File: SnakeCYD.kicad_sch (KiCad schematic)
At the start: 1 part, among them U2 TFT_320x240

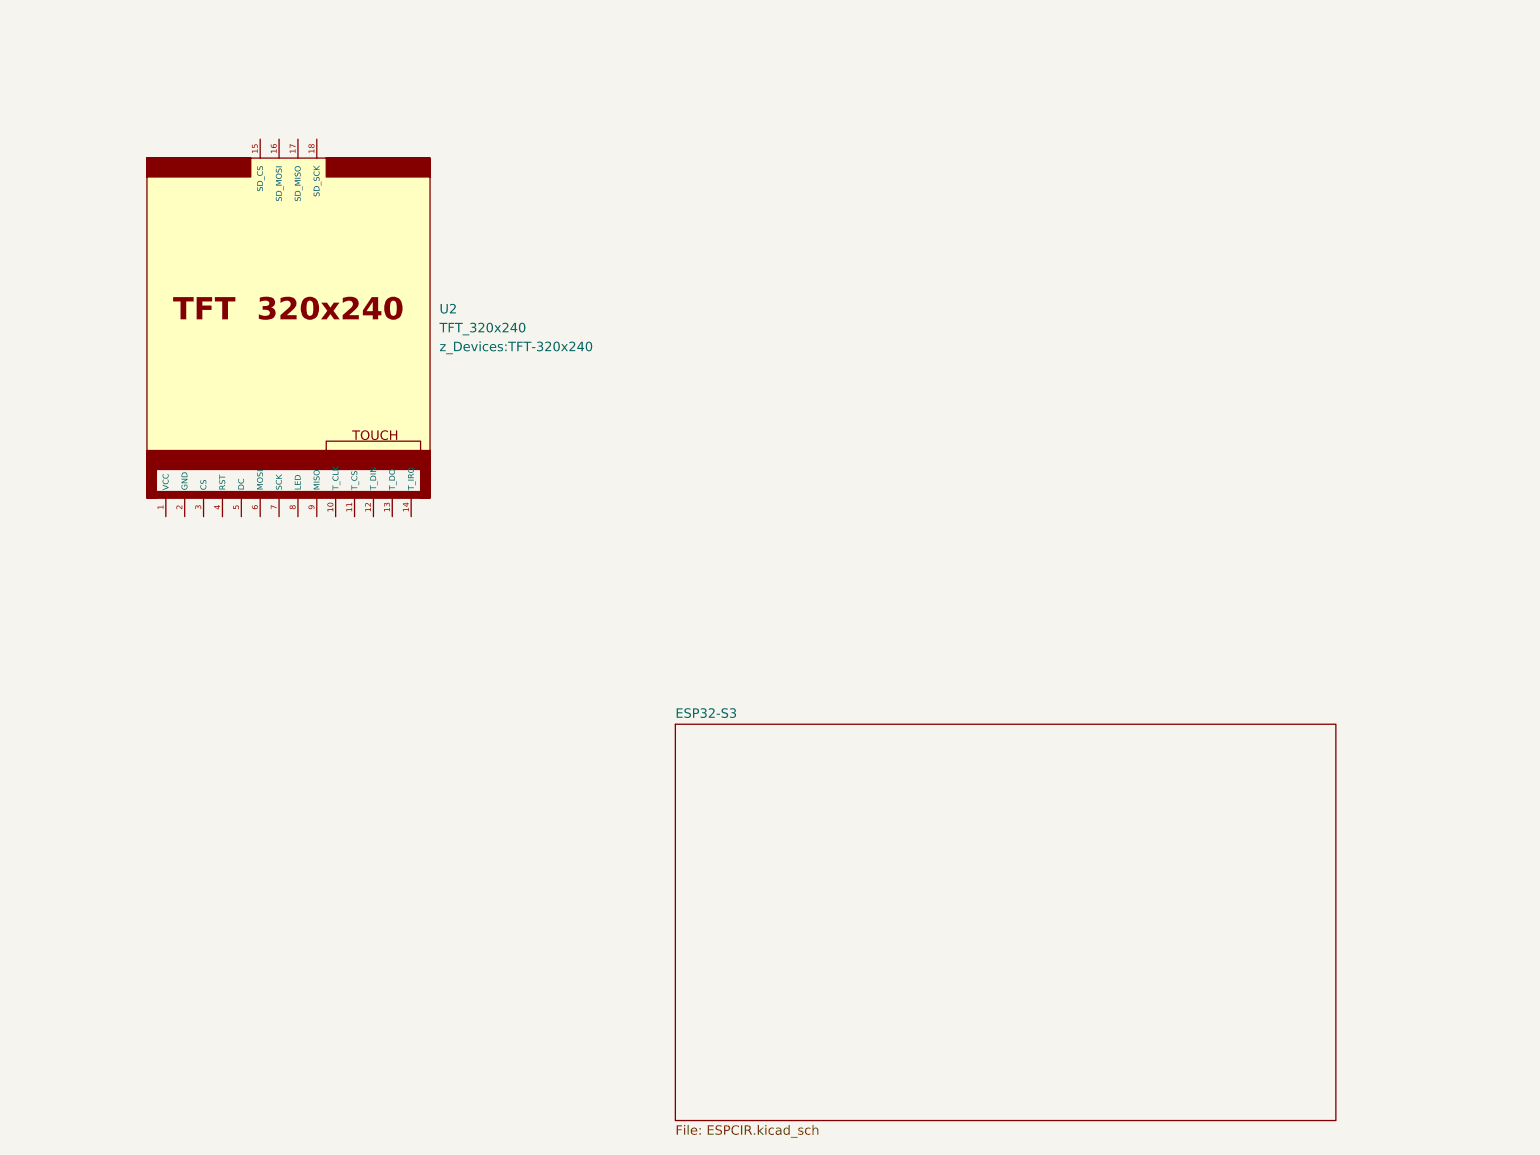
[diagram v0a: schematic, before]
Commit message: Wired the tft screen (Schem)
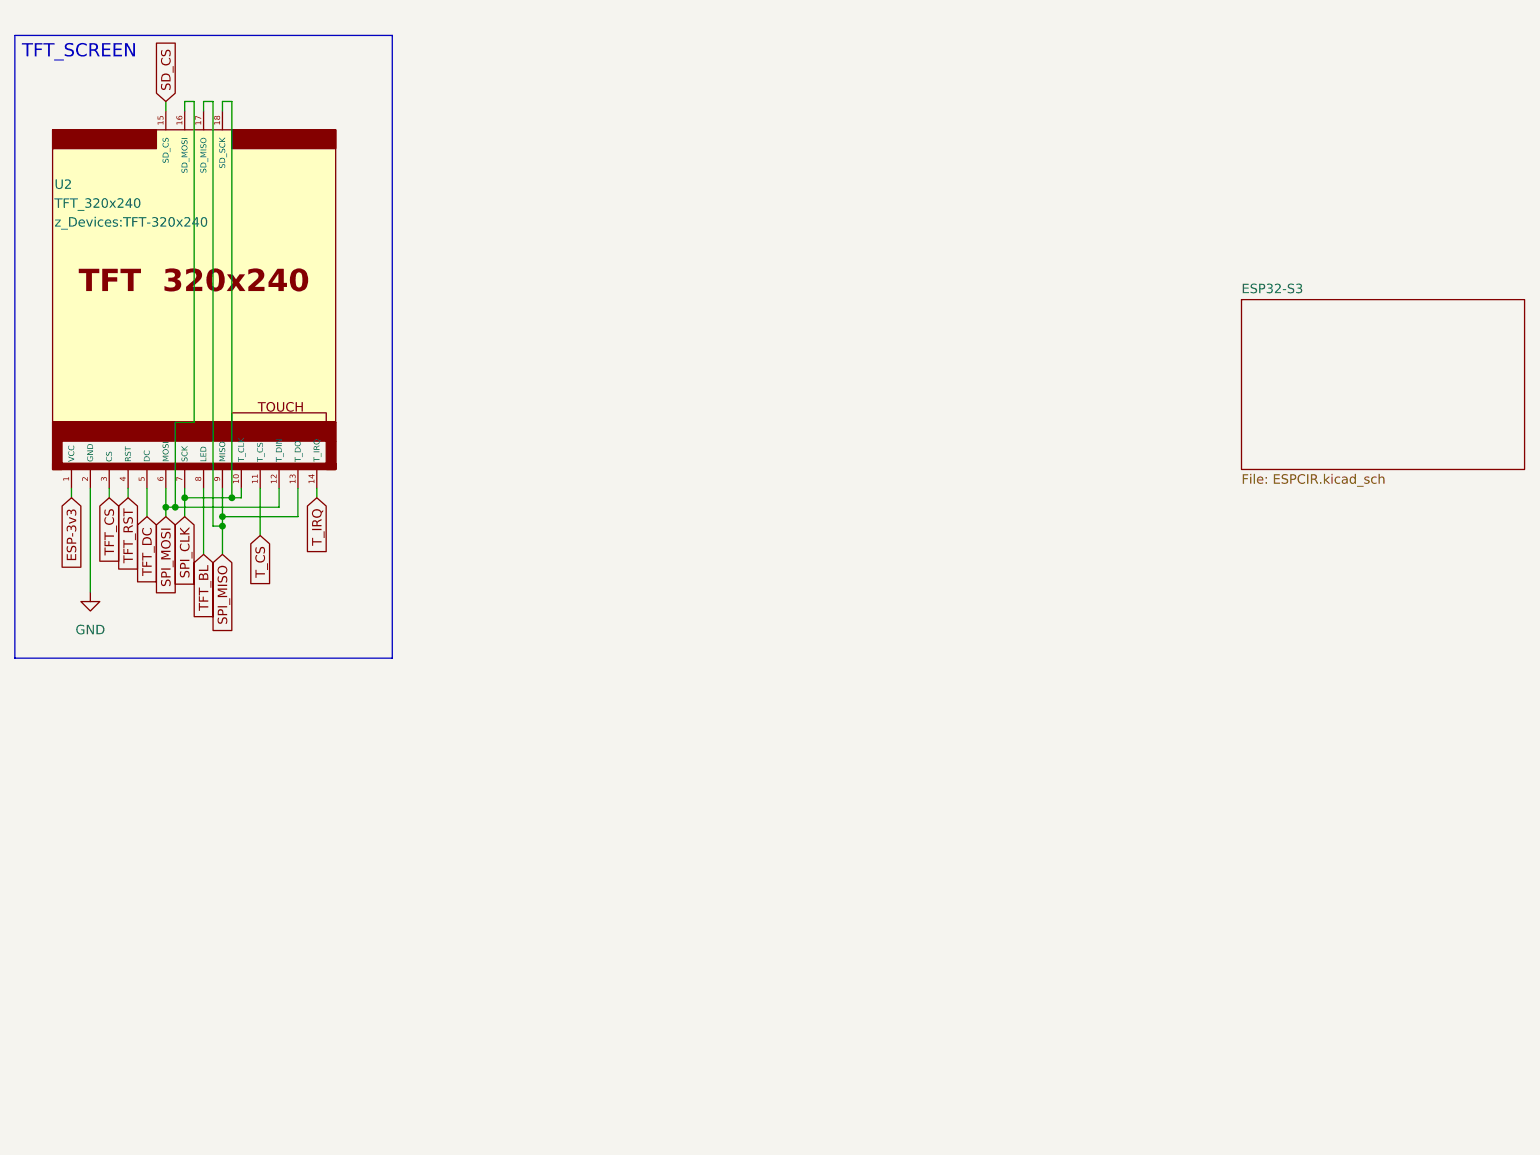
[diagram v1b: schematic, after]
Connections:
- net ESP-3v3: now reaches U2.1 (VCC)
- net SPI_CLK: now reaches U2.10 (T_CLK)
- net SPI_CLK: now also U2.18 (SD_SCK), U2.7 (SCK)
- net T_CS: now reaches U2.11 (T_CS)
- net SPI_MOSI: now reaches U2.12 (T_DIN)
- net SPI_MOSI: now also U2.16 (SD_MOSI), U2.6 (MOSI)
- net SPI_MISO: now reaches U2.13 (T_DO)
- net SPI_MISO: now also U2.17 (SD_MISO), U2.9 (MISO)
- net T_IRQ: now reaches U2.14 (T_IRQ)
- net SD_CS: now reaches U2.15 (SD_CS)
- net GND: now reaches U2.2 (GND)
- net TFT_CS: now reaches U2.3 (CS)
- net TFT_RST: now reaches U2.4 (RST)
- net TFT_DC: now reaches U2.5 (DC)
- net TFT_BL: now reaches U2.8 (LED)
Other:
- moved on the sheet: U2

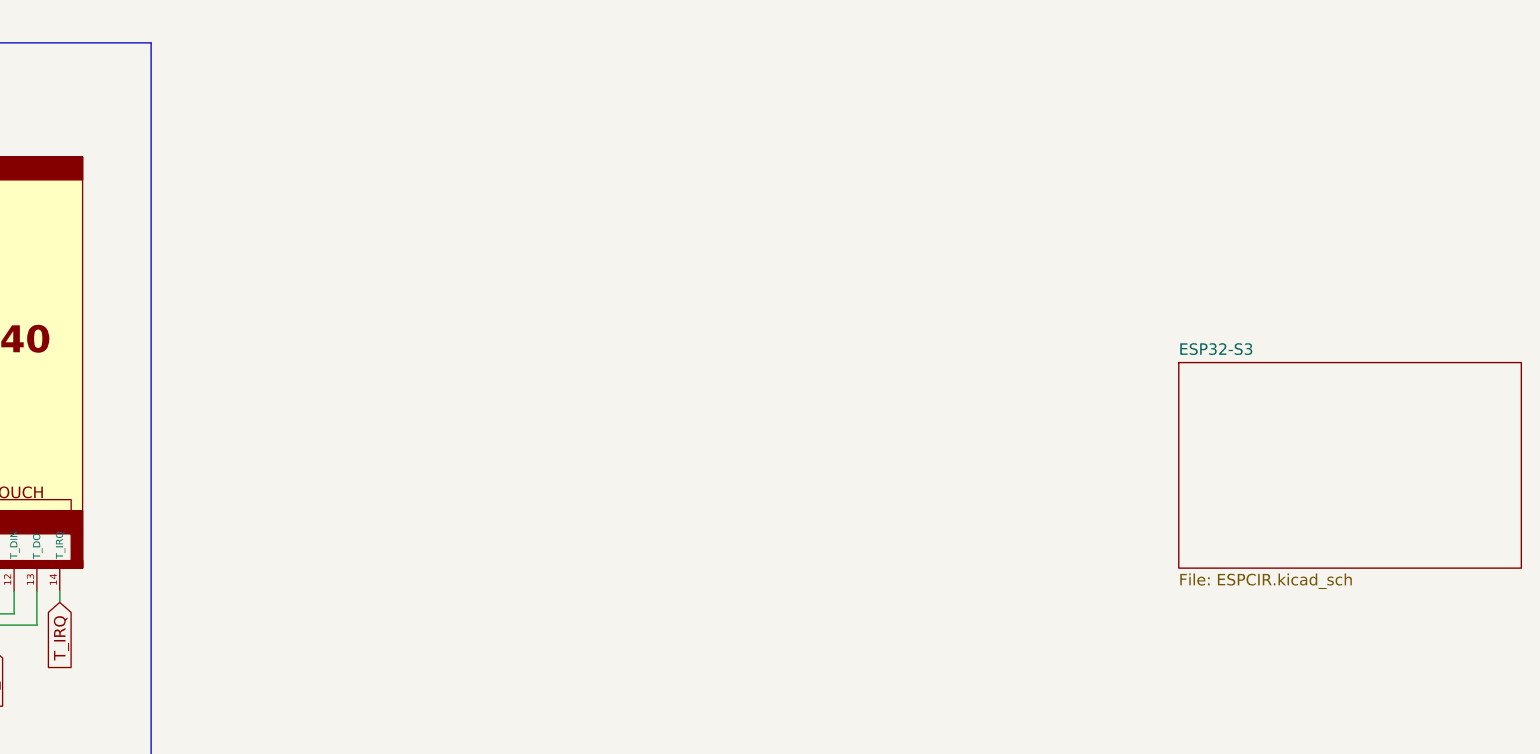
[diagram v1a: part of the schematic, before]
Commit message: Assigned all the avaliable pins from the esp32 s3 gpio to labels (Schem)
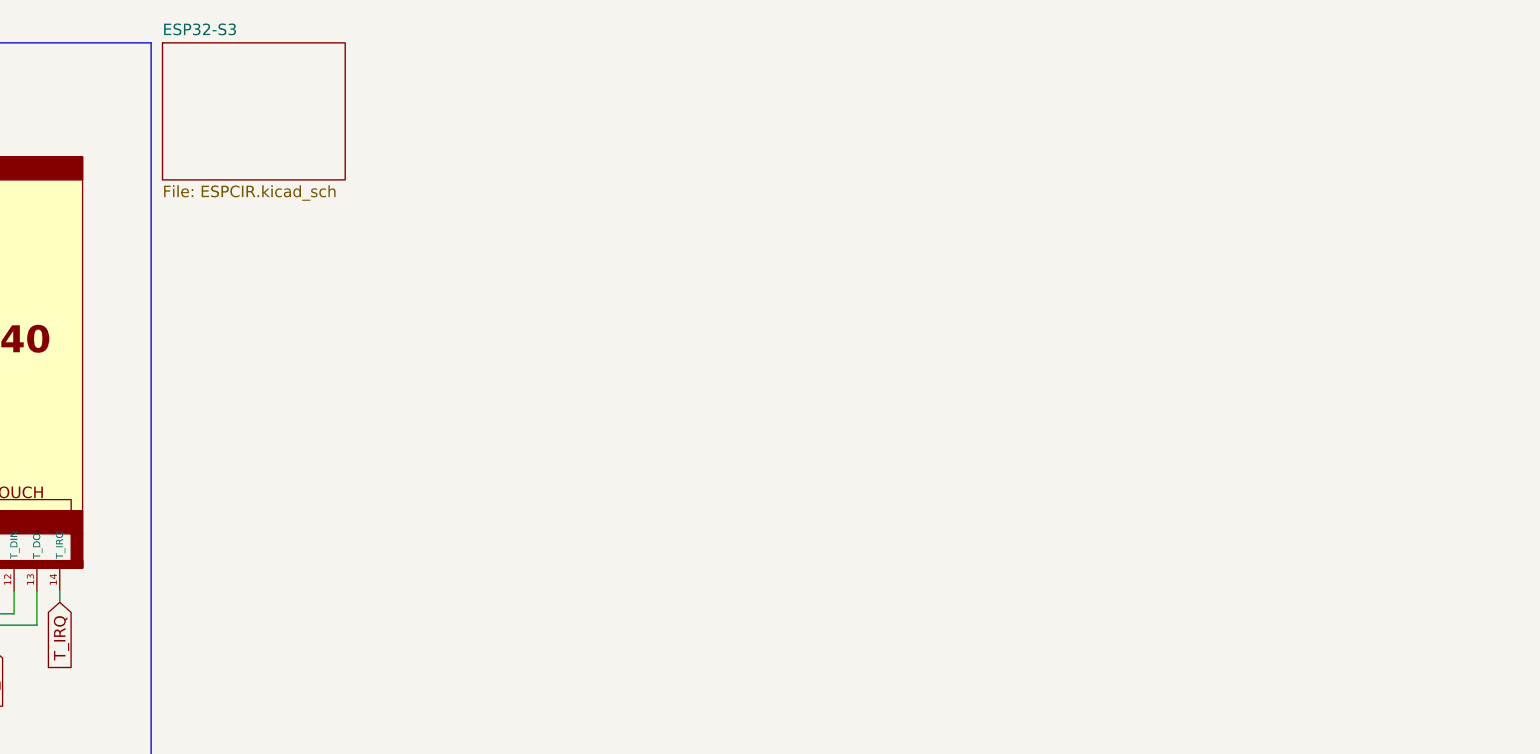
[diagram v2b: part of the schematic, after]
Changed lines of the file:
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@@
 	)
 	(sheet
-		(at 180.34 52.07)
-		(size 38.1 22.86)
+		(at 67.31 16.51)
+		(size 20.32 15.24)
 		(exclude_from_sim no)
 		(in_bom yes)
@@
 		)
 		(property "Sheetname" "ESP32-S3"
-			(at 180.34 51.3584 0)
+			(at 67.31 15.7984 0)
 			(show_name no)
 			(do_not_autoplace no)
@@
 		)
 		(property "Sheetfile" "ESPCIR.kicad_sch"
-			(at 180.34 75.5146 0)
+			(at 67.31 32.3346 0)
 			(show_name no)
 			(do_not_autoplace no)

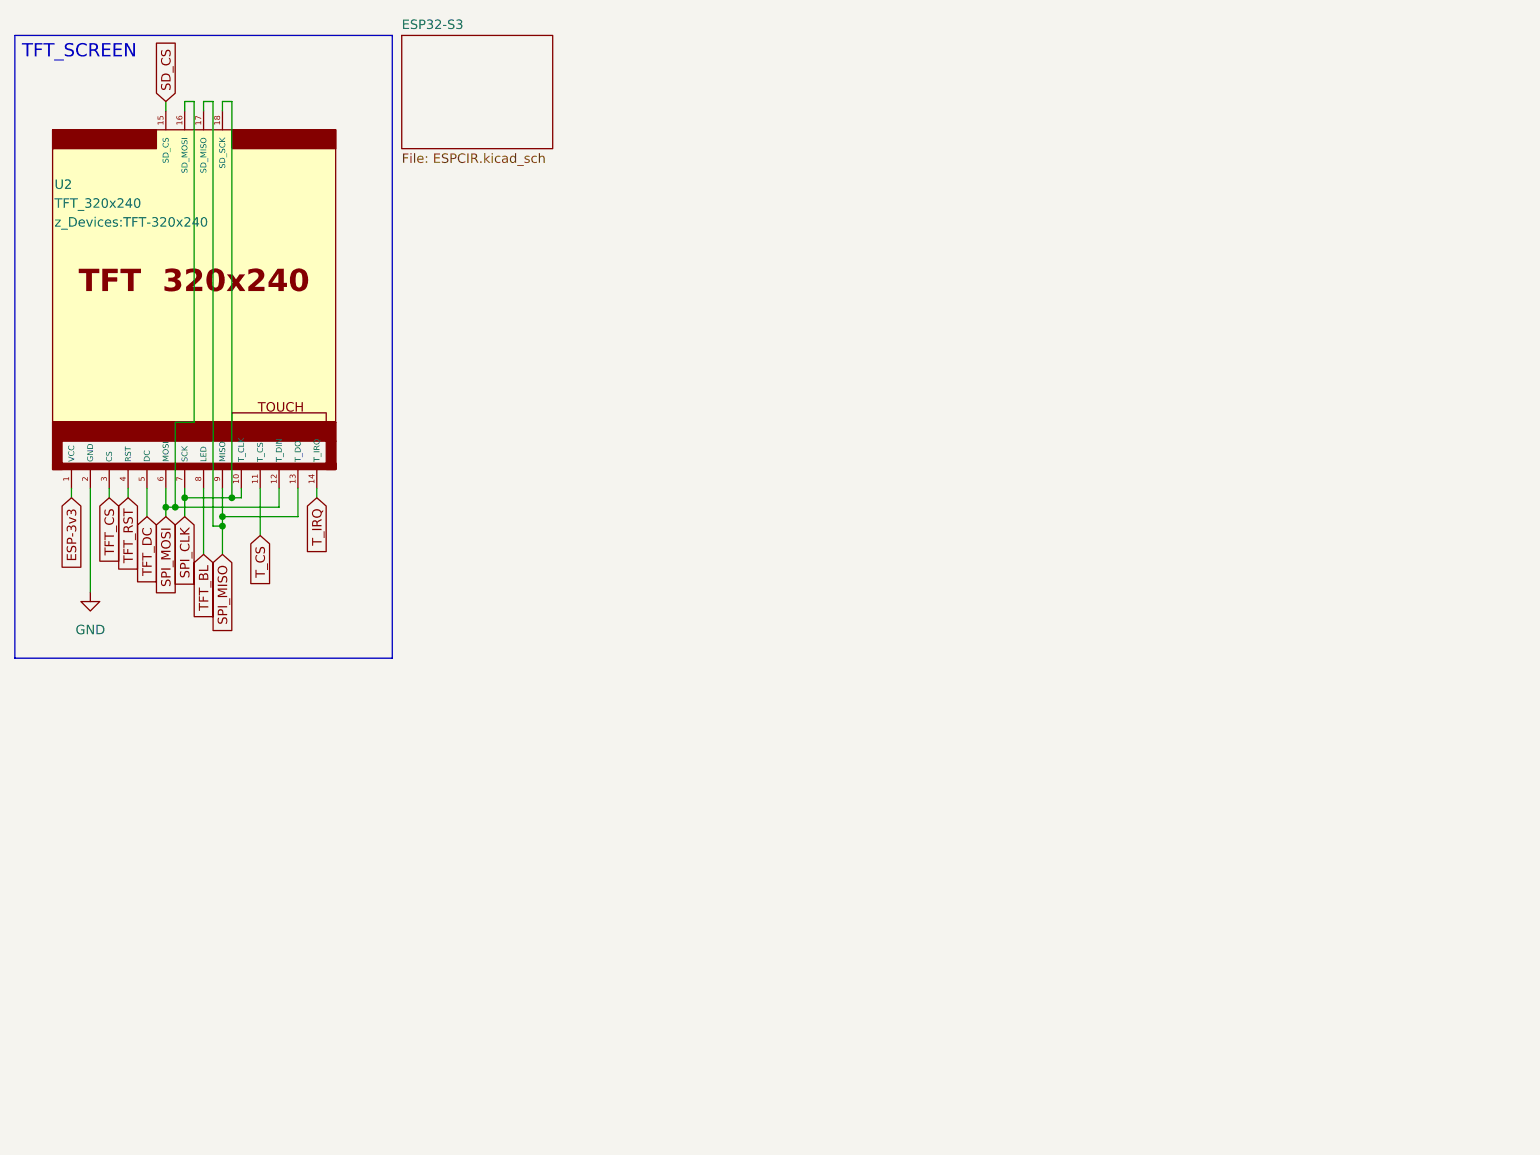
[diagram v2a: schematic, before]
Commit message: (Likely finished the Schem) Wired all the connectors and esp pins
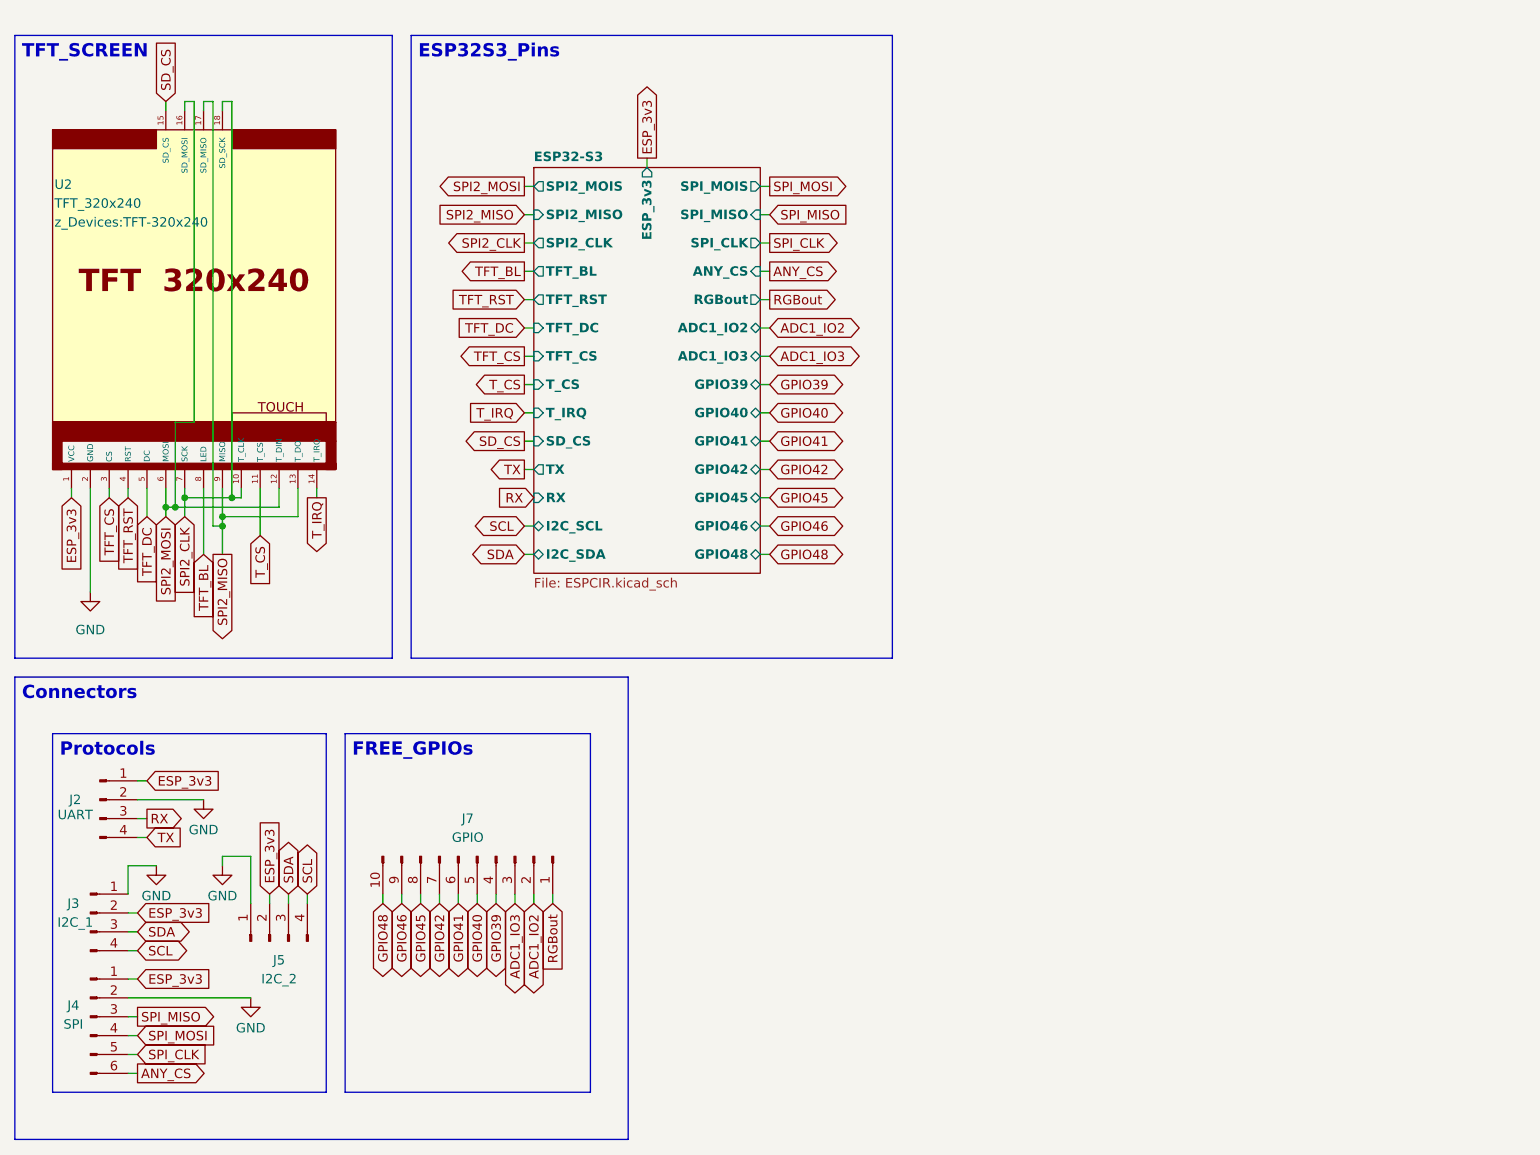
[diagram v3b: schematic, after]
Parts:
- added J2: UART, symbol Connector:Conn_01x04_Pin
- added J3: I2C_1, symbol Connector:Conn_01x04_Pin
- added J4: SPI, symbol Connector:Conn_01x06_Pin
- added J5: I2C_2, symbol Connector:Conn_01x04_Pin
- added J7: GPIO, symbol Connector:Conn_01x10_Pin
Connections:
- net GND: now also J2.2 (Pin_2), J3.1 (Pin_1), J4.2 (Pin_2), J5.1 (Pin_1)
- net SPI_CLK: now also J4.5 (Pin_5); no longer U2.10 (T_CLK), U2.18 (SD_SCK), U2.7 (SCK)
- net SPI_MISO: now also J4.3 (Pin_3); no longer U2.13 (T_DO), U2.17 (SD_MISO), U2.9 (MISO)
- net SPI_MOSI: now also J4.4 (Pin_4); no longer U2.12 (T_DIN), U2.16 (SD_MOSI), U2.6 (MOSI)
- net ESP-3v3 renamed ESP_3v3
- net ESP_3v3: now also J2.1 (Pin_1), J3.2 (Pin_2), J4.1 (Pin_1), J5.2 (Pin_2)
- new net ADC1_IO2: J7.2 (Pin_2)
- new net ADC1_IO3: J7.3 (Pin_3)
- new net ANY_CS: J4.6 (Pin_6)
- new net GPIO39: J7.4 (Pin_4)
- new net GPIO40: J7.5 (Pin_5)
- new net GPIO41: J7.6 (Pin_6)
- new net GPIO42: J7.7 (Pin_7)
- new net GPIO45: J7.8 (Pin_8)
- new net GPIO46: J7.9 (Pin_9)
- new net GPIO48: J7.10 (Pin_10)
- new net RGBout: J7.1 (Pin_1)
- new net RX: J2.3 (Pin_3)
- new net SCL: J3.4 (Pin_4), J5.4 (Pin_4)
- new net SDA: J3.3 (Pin_3), J5.3 (Pin_3)
- new net SPI2_CLK: U2.10 (T_CLK), U2.18 (SD_SCK), U2.7 (SCK)
- new net SPI2_MISO: U2.13 (T_DO), U2.17 (SD_MISO), U2.9 (MISO)
- new net SPI2_MOSI: U2.12 (T_DIN), U2.16 (SD_MOSI), U2.6 (MOSI)
- new net TX: J2.4 (Pin_4)
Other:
- sheet ESP32-S3 ports: added ADC1_IO2, ADC1_IO3, ANY_CS, ESP_3v3, GPIO39, GPIO40, GPIO41, GPIO42, GPIO45, GPIO46, GPIO48, I2C_SCL, I2C_SDA, RGBout, RX, SD_CS, SPI2_CLK, SPI2_MISO, SPI2_MOIS, SPI_CLK, SPI_MISO, SPI_MOIS, TFT_BL, TFT_CS, TFT_DC, TFT_RST, TX, T_CS, T_IRQ; removed none

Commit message: Fully Finshed the schem
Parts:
- added J6: 0UART, Connector_JST:JST_XH_S4B-XH-A-1_1x04_P2.50mm_Horizontal, symbol Connector:Conn_01x04_Pin
- J2, J3, J5: footprint (none) -> Connector_JST:JST_XH_S4B-XH-A-1_1x04_P2.50mm_Horizontal
- J4: footprint (none) -> Connector_JST:JST_XH_S6B-XH-A-1_1x06_P2.50mm_Horizontal
- J7: footprint (none) -> Connector_PinSocket_2.54mm:PinSocket_1x10_P2.54mm_Horizontal
- U2: footprint z_Devices:TFT-320x240 -> Display-extra:TFT-320x240
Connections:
- net ESP_3v3: now also J6.1 (Pin_1)
- net GND: now also J6.2 (Pin_2)
- new net 0RX: J6.3 (Pin_3)
- new net 0TX: J6.4 (Pin_4)
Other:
- sheet ESP32-S3 ports: added 0RX, 0TX; removed none
- moved on the sheet: J5, J7
